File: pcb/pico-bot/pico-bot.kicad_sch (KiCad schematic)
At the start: 52 parts

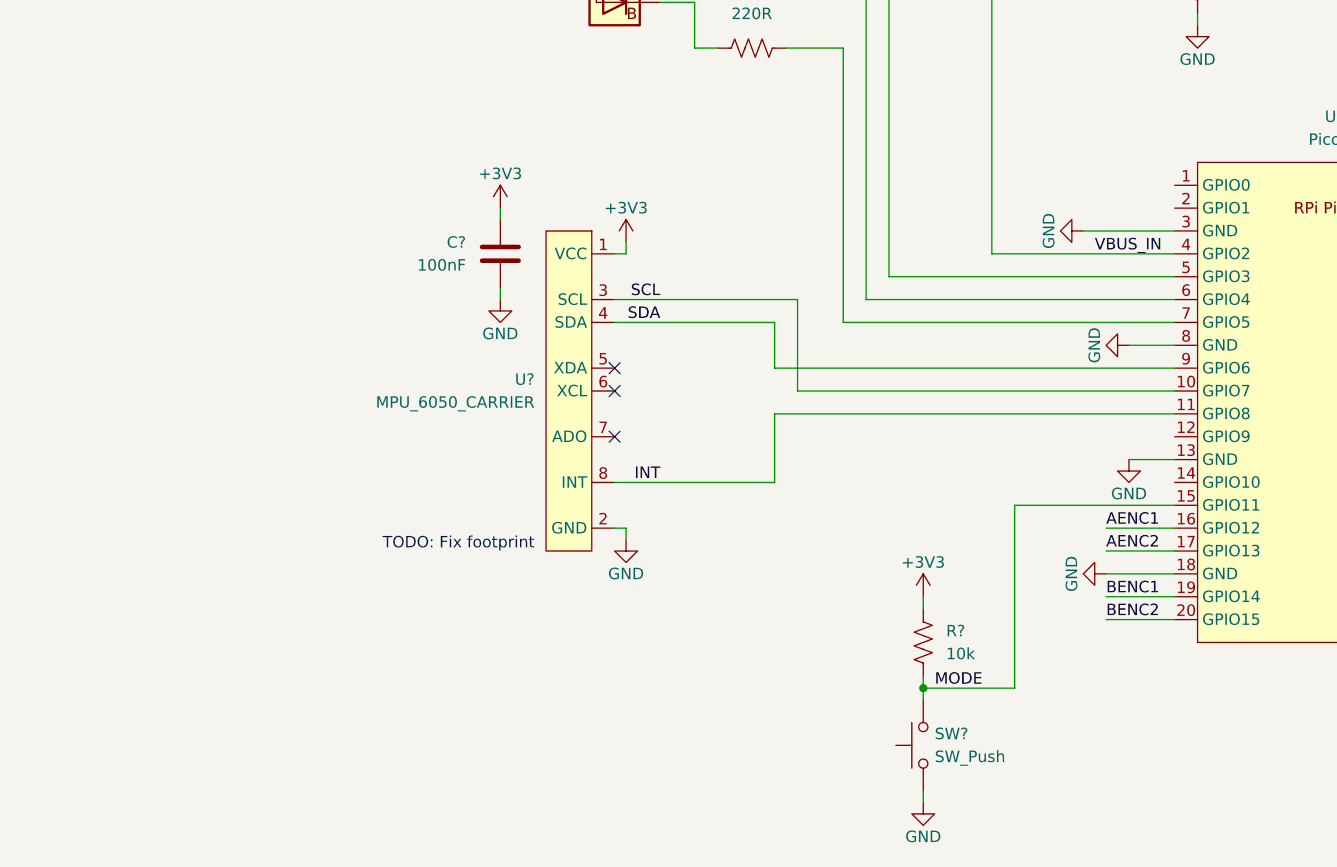
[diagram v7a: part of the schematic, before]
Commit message: Use mpu6050 directly instead of carrier board
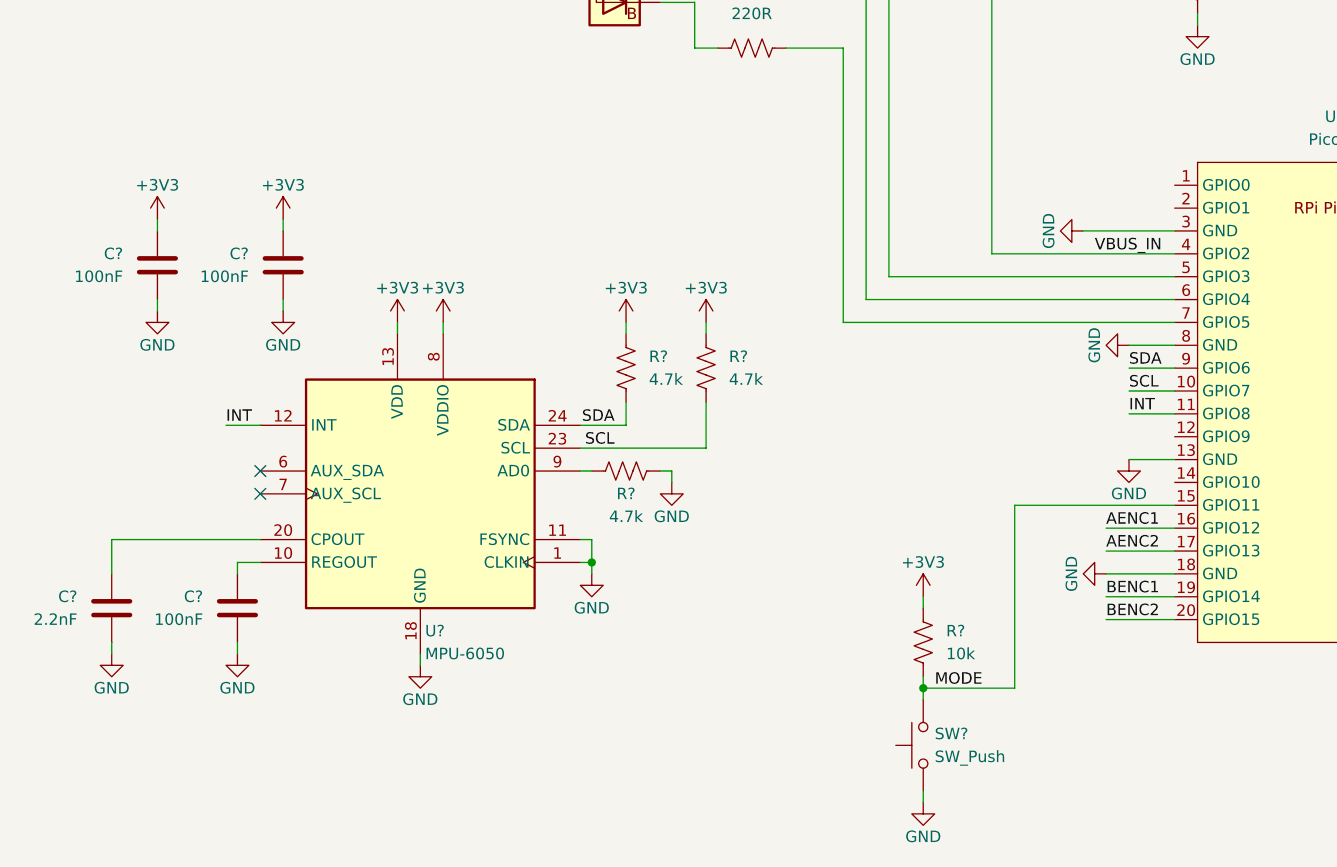
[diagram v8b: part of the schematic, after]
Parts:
- removed C?: 100nF, Capacitor_SMD:C_0805_2012Metric_Pad1.18x1.45mm_HandSolder, symbol Device:C
- removed U?: MPU_6050_CARRIER, symbol pico-bot:MPU_6050_CARRIER
- added C? (x3): 100nF, Capacitor_SMD:C_0805_2012Metric_Pad1.18x1.45mm_HandSolder, symbol Device:C
- added C?: 2.2nF, Capacitor_SMD:C_0805_2012Metric_Pad1.18x1.45mm_HandSolder, symbol Device:C
- added R? (x3): 4.7k, Resistor_SMD:R_0805_2012Metric_Pad1.20x1.40mm_HandSolder, symbol Device:R_US
- added U?: MPU-6050, Sensor_Motion:InvenSense_QFN-24_4x4mm_P0.5mm, symbol Sensor_Motion:MPU-6050
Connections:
- net +3V3: now also C?.2, C?.2, R?.2, R?.2, U?.13 (VDD), U?.8 (VDDIO)
- net GND: now also C?.1, C?.1, C?.1, C?.1, R?.1, U?.1 (CLKIN), U?.11 (FSYNC), U?.18 (GND)
- net INT: now also U?.12 (INT)
- net SCL: now also R?.1, U?.23 (SCL)
- net SDA: now also R?.1, U?.24 (SDA)
- new net: C?.2, U?.10 (REGOUT)
- new net: R?.2, U?.9 (AD0)
- new net: C?.2, U?.20 (CPOUT)
- no-connect marks 4 -> 3
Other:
- note removed: "TODO: Fix footprint"
